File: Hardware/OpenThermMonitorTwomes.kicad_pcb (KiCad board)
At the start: 2 copper layers, 31.1 x 34.5 mm, 28 parts, among them J1 Boiler, J2 Therm, P1 CONN_01X08, P2 CONN_01X08, SW1 SW_Push, U1 HT7550-1, U2 LM393DR2G, U3 EL357N(C), U4 EL357N(C)

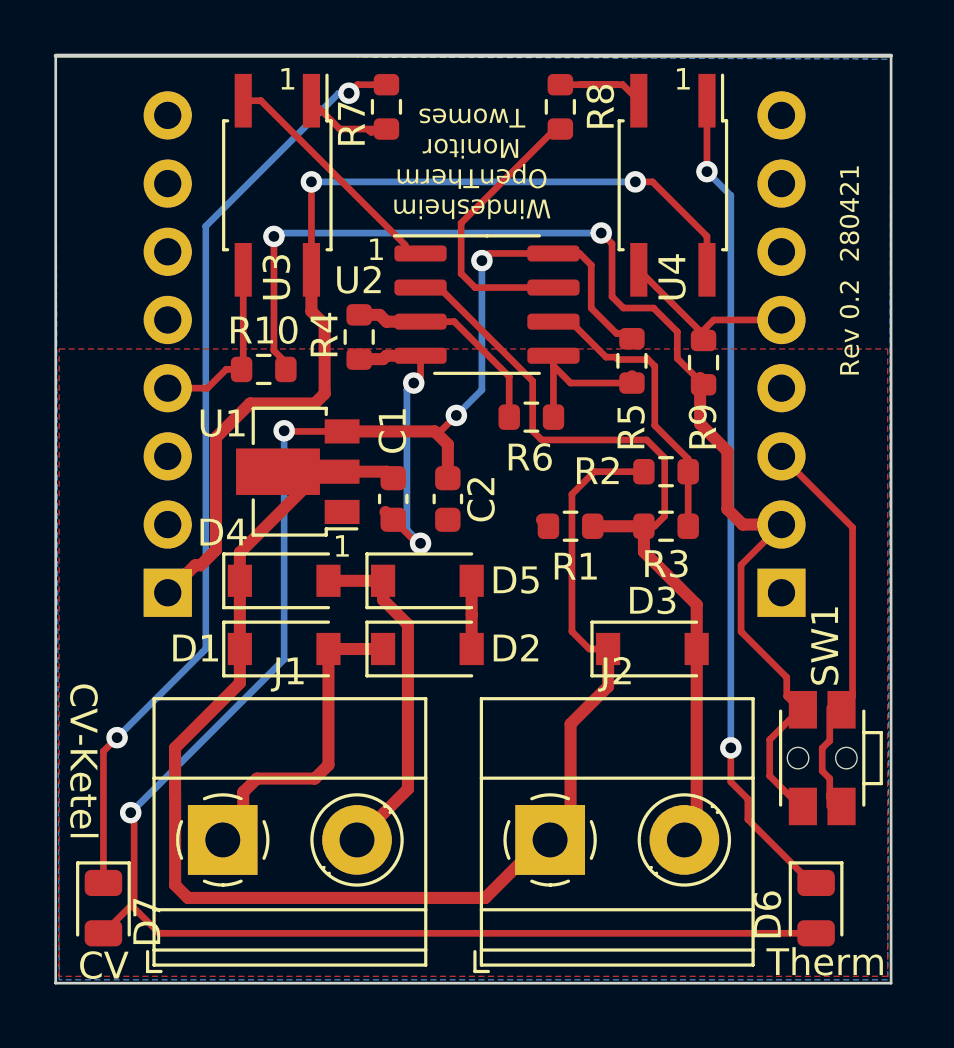
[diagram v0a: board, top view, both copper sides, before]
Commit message: V1.1 Fixed risetime issue
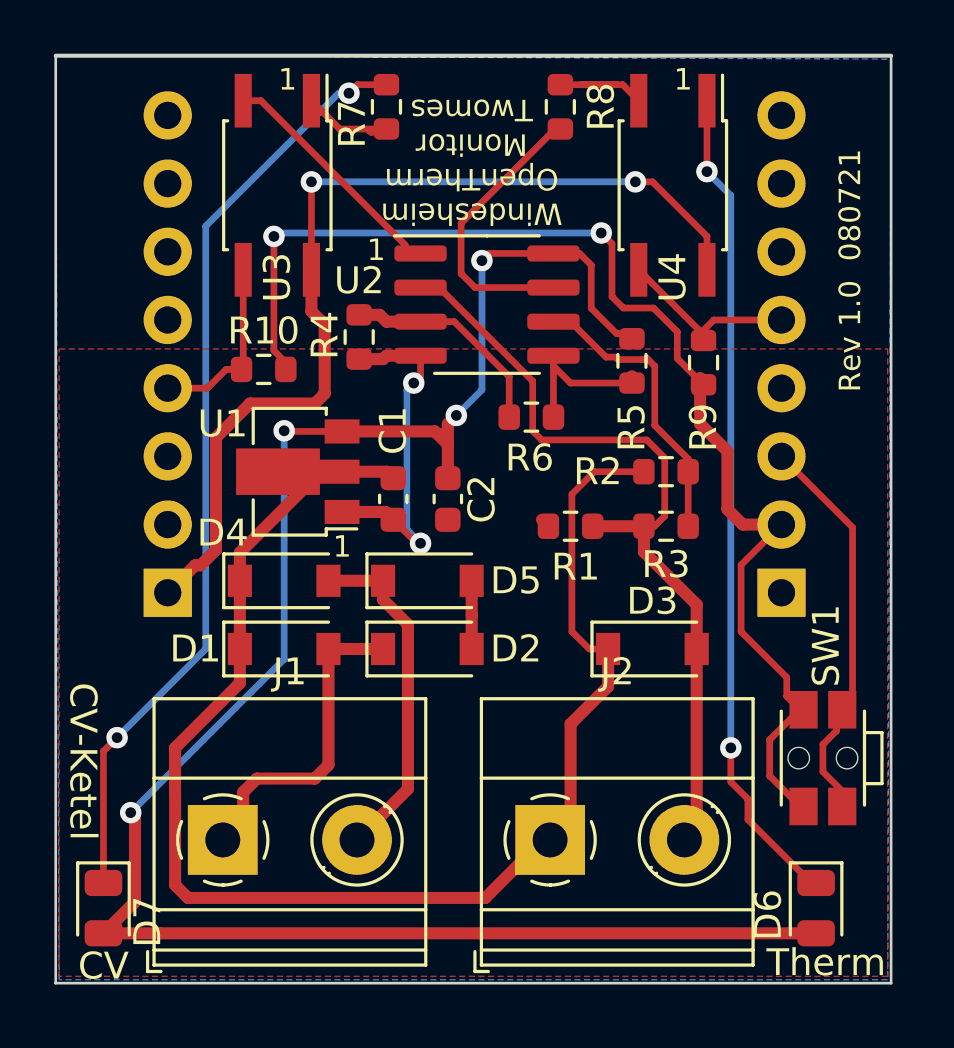
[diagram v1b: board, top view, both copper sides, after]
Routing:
- net GND1: track 14.9 -> 16.5 mm
- net /5V: track 70.6 -> 71.6 mm
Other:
- board text added: "CS"
- board text added: "Licensed under CERN-OHL-P v2"
- board text added: "MISO"
- board text added: "MOSI"
- board text added: "RST"
- board text added: "Rev 1.0 080721"
- board text added: "SCK"
- board text added: "SCL"
- board text added: "SDA"
- board text removed: "D1"
- board text removed: "D2"
- board text removed: "D5"
- board text removed: "D6"
- board text removed: "D7"
- board text removed: "D8"
- board text removed: "Rev 0.2 280421"
- board text removed: "Rst"

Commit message: Generated new position files for PCB assembly to reflect updated components in v1.1 schematic
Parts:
- C1: value 100nF -> 10nF
- R8: value 470R -> 1k
